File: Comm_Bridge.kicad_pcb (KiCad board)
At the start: 2 copper layers, 66 x 55.9 mm, 98 parts, among them P1 USB_B, P2 CONN_01X03, P3 Solenoid, P4 XT60, P5 CONN_01X03, P6 CONN_01X03, U1 FT4232H, U10 ADM3251E, U11 ADM3251E, U2 93LC56BT-I/OT, U3 74HC595_CUST, U4 LM1117-XX, U5 ADC101S021, U6 NLSX4373, U7 NLSX4373, U8 ACPL-247-500E, U9 ACPL-247-500E, Y1 12MHz

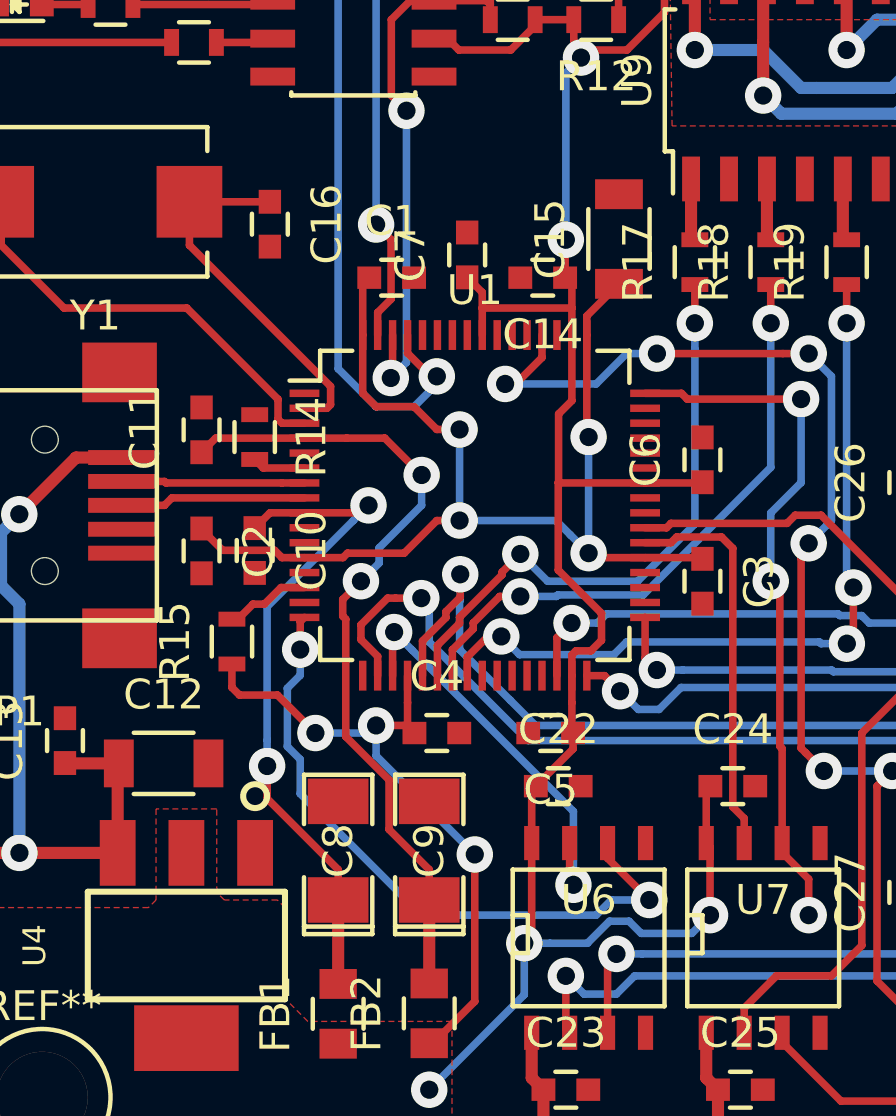
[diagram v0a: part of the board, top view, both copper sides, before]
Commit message: Change the PCB footprints of C4.7uF and 3.3uF from 1206 to 0803 (smaller)
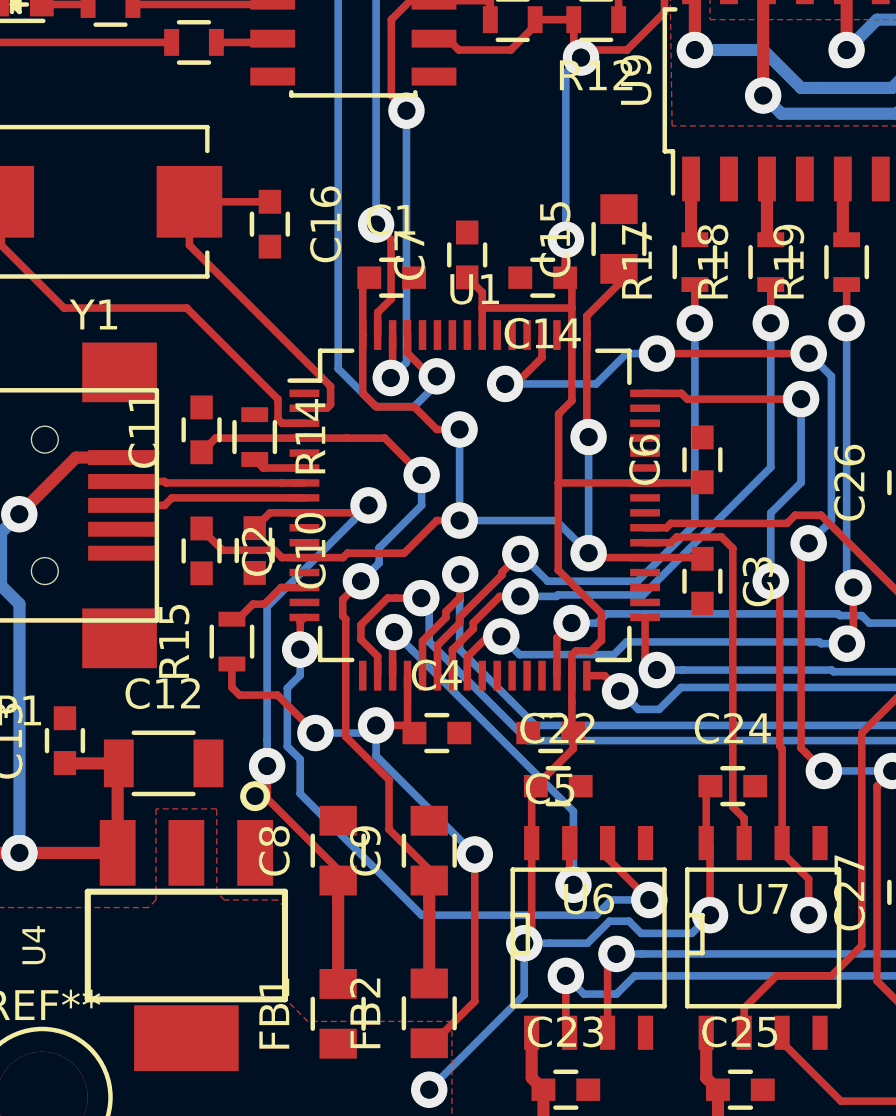
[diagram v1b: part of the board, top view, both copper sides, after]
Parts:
- C15: footprint Capacitors_SMD:C_1206 -> Capacitors_SMD:C_0805
- C8, C9: footprint SMD_Packages:SMD-1206_Pol -> Capacitors_SMD:C_0805
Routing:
- net +1V8: track 38.5 -> 39.0 mm

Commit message: Change the version of KiCad to 4.0.6 and un-connected ID_Pin of the USB connector.
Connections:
- P1 pad 4: GND -> Net-(P1-Pad4)
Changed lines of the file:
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@@
-(kicad_pcb (version 4) (host pcbnew 4.0.5)
+(kicad_pcb (version 4) (host pcbnew 4.0.6)
   (general
-    (links 252)
+    (links 251)
     (no_connects 0)
     (area 118.2798 76.124999 185.785401 132.232402)
@@
     (zones 0)
     (modules 98)
-    (nets 113)
+    (nets 114)
   )
   (page A4)
@@
   (net 111 "Net-(U1-Pad59)")
   (net 112 "Net-(U1-Pad60)")
+  (net 113 "Net-(P1-Pad4)")
   (net_class Default "This is the default net class."
     (clearance 0.2032)
@@
     (add_net "Net-(P1-Pad2)")
     (add_net "Net-(P1-Pad3)")
+    (add_net "Net-(P1-Pad4)")
     (add_net "Net-(P5-Pad2)")
     (add_net "Net-(P5-Pad3)")
@@
       (net 42 "Net-(P1-Pad3)"))
     (pad 4 smd rect (at 3.44932 0.8001) (size 2.30124 0.50038) (layers F.Cu F.Paste F.Mask)
-      (net 2 GND))
+      (net 113 "Net-(P1-Pad4)"))
     (pad 5 smd rect (at 3.44932 1.6002) (size 2.30124 0.50038) (layers F.Cu F.Paste F.Mask)
       (net 2 GND))

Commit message: Merge branch 'Peripheral_Bridge'
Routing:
- net GND: track 8.38 -> 69.5 mm
- net Net-(R13-Pad1): track 30.1 -> 31.9 mm
- net VBUS: track 181.5 -> 180.0 mm
- net Net-(R11-Pad1): track 23.4 -> 24.5 mm
- net Net-(C10-Pad1): track 22.5 -> 21.6 mm
- net Net-(C11-Pad1): track 27.4 -> 26.6 mm

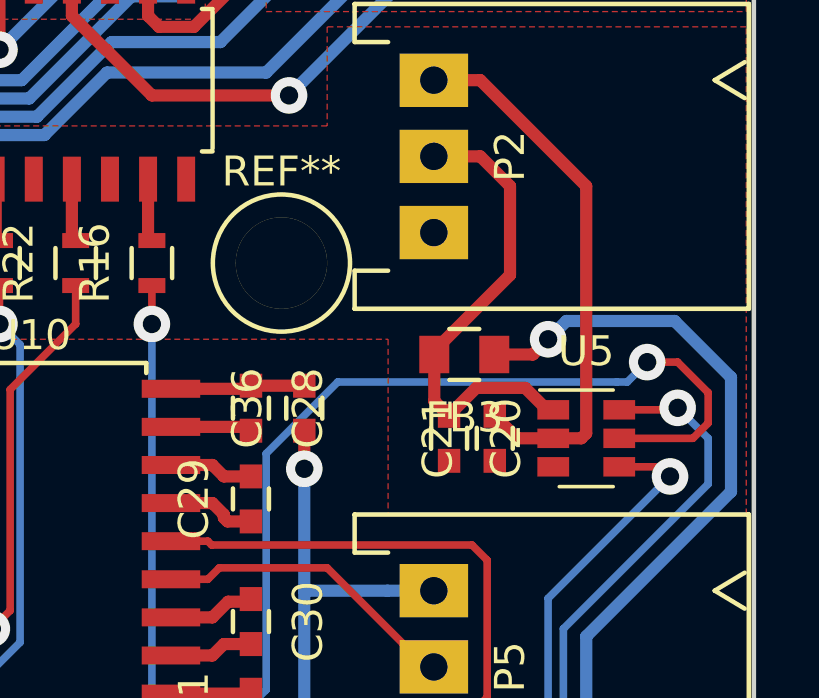
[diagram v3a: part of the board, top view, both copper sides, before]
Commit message: ADC bug fixed
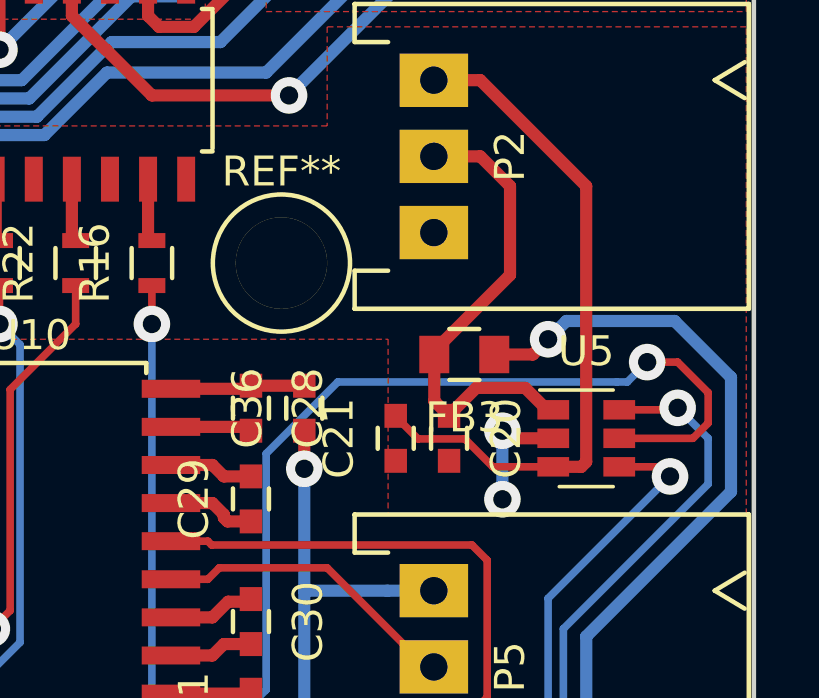
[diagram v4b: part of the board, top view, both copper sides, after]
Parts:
- moved C21 3.30 mm to (173.5, 104.6)
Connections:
- U5 pad 2: Net-(C21-Pad2) -> GND
- U5 pad 3: GND -> Net-(C21-Pad2)
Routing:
- net Net-(C21-Pad2): track 18.2 -> 22.9 mm
- net GND: track 69.5 -> 73.6 mm, vias 2 -> 4
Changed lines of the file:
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@@
     (thickness 1.6)
     (drawings 5)
-    (tracks 888)
+    (tracks 896)
     (zones 0)
     (modules 98)
@@
   )
   (setup
-    (last_trace_width 0.254)
+    (last_trace_width 0.4064)
     (user_trace_width 0.4064)
     (user_trace_width 1.27)
@@
   )
   (module Capacitors_SMD:C_0603 (layer F.Cu)
-    (at 176.784 104.648 90)
+    (at 173.482 104.648 90)
     (descr "Capacitor SMD 0603, reflow soldering, AVX (see smccp.pdf)")
     (tags "capacitor 0603")
@@
       (net 7 "Net-(C20-Pad1)"))
     (pad 2 smd rect (at -1.1 0) (size 1.06 0.65) (layers F.Cu F.Paste F.Mask)
-      (net 8 "Net-(C21-Pad2)"))
-    (pad 3 smd rect (at -1.1 0.95) (size 1.06 0.65) (layers F.Cu F.Paste F.Mask)
       (net 2 GND))
+    (pad 3 smd rect (at -1.1 0.95) (size 1.06 0.65) (layers F.Cu F.Paste F.Mask)
+      (net 8 "Net-(C21-Pad2)"))
     (pad 4 smd rect (at 1.1 0.95) (size 1.06 0.65) (layers F.Cu F.Paste F.Mask)
       (net 77 "Net-(U5-Pad4)"))
@@
   (segment (start 133.246 108.684) (end 133.000201 108.438201) (width 0.254) (layer F.Cu) (net 1))
   (segment (start 131.261201 108.438201) (end 130.556 107.733) (width 0.254) (layer F.Cu) (net 1))
+  (segment (start 177.038 104.394) (end 177.038 106.68) (width 0.4064) (layer B.Cu) (net 2))
+  (via (at 177.038 106.68) (size 1.2192) (drill 0.6096) (layers F.Cu B.Cu) (net 2))
+  (segment (start 178.732 104.648) (end 177.292 104.648) (width 0.4064) (layer F.Cu) (net 2))
+  (segment (start 177.292 104.648) (end 177.038 104.394) (width 0.4064) (layer F.Cu) (net 2))
+  (via (at 177.038 104.394) (size 1.2192) (drill 0.6096) (layers F.Cu B.Cu) (net 2))
   (segment (start 149.710138 123.444) (end 150.4315 123.444) (width 0.254) (layer F.Cu) (net 2))
   (segment (start 151.257 124.2695) (end 151.257 124.587) (width 0.254) (layer F.Cu) (net 2))
@@
   (segment (start 174.768 101.854) (end 174.768 103.406) (width 0.4064) (layer F.Cu) (net 7))
   (segment (start 174.768 103.406) (end 175.26 103.898) (width 0.4064) (layer F.Cu) (net 7))
-  (segment (start 179.832 96.2406) (end 179.832 104.4844) (width 0.4064) (layer F.Cu) (net 8))
-  (segment (start 179.832 104.4844) (end 179.6684 104.648) (width 0.4064) (layer F.Cu) (net 8))
-  (segment (start 179.6684 104.648) (end 178.732 104.648) (width 0.4064) (layer F.Cu) (net 8))
+  (segment (start 175.787799 104.667799) (end 176.718 105.598) (width 0.254) (layer F.Cu) (net 8))
+  (segment (start 176.718 105.598) (end 178.732 105.598) (width 0.254) (layer F.Cu) (net 8))
+  (segment (start 173.482 103.898) (end 173.482 103.923) (width 0.254) (layer F.Cu) (net 8))
+  (segment (start 173.482 103.923) (end 174.226799 104.667799) (width 0.254) (layer F.Cu) (net 8))
+  (segment (start 174.226799 104.667799) (end 175.787799 104.667799) (width 0.254) (layer F.Cu) (net 8))
+  (segment (start 179.832 96.2406) (end 179.832 105.4344) (width 0.4064) (layer F.Cu) (net 8))
+  (segment (start 179.832 105.4344) (end 179.6684 105.598) (width 0.4064) (layer F.Cu) (net 8))
+  (segment (start 179.6684 105.598) (end 178.732 105.598) (width 0.4064) (layer F.Cu) (net 8))
   (segment (start 174.752 92.71) (end 176.3014 92.71) (width 0.4064) (layer F.Cu) (net 8))
   (segment (start 176.3014 92.71) (end 179.832 96.2406) (width 0.4064) (layer F.Cu) (net 8))
-  (segment (start 176.784 103.898) (end 177.534 104.648) (width 0.4064) (layer F.Cu) (net 8))
-  (segment (start 177.534 104.648) (end 178.732 104.648) (width 0.4064) (layer F.Cu) (net 8))
   (segment (start 168.656 102.894) (end 170.434 102.894) (width 0.4064) (layer F.Cu) (net 9))
   (segment (start 165.99 102.997) (end 168.553 102.997) (width 0.4064) (layer F.Cu) (net 9))

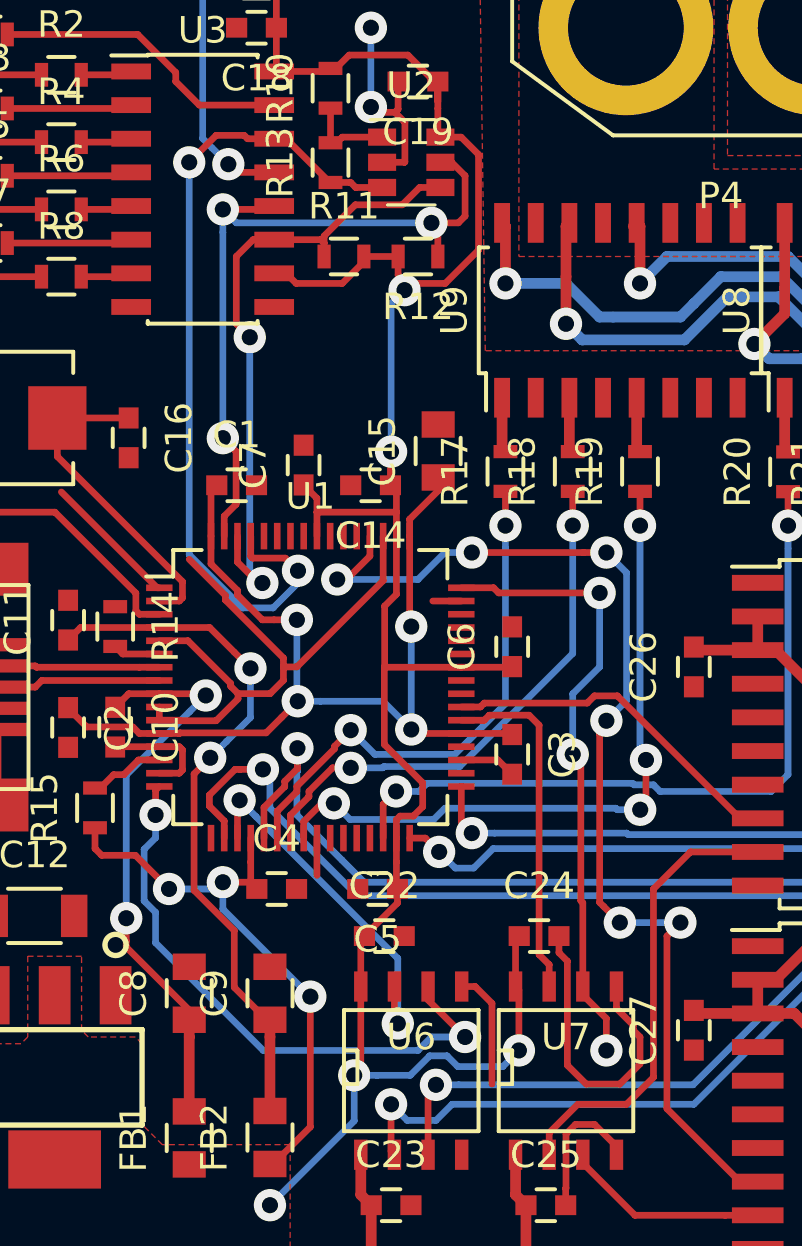
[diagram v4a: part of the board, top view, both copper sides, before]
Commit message: Bug fixed at 74HC595
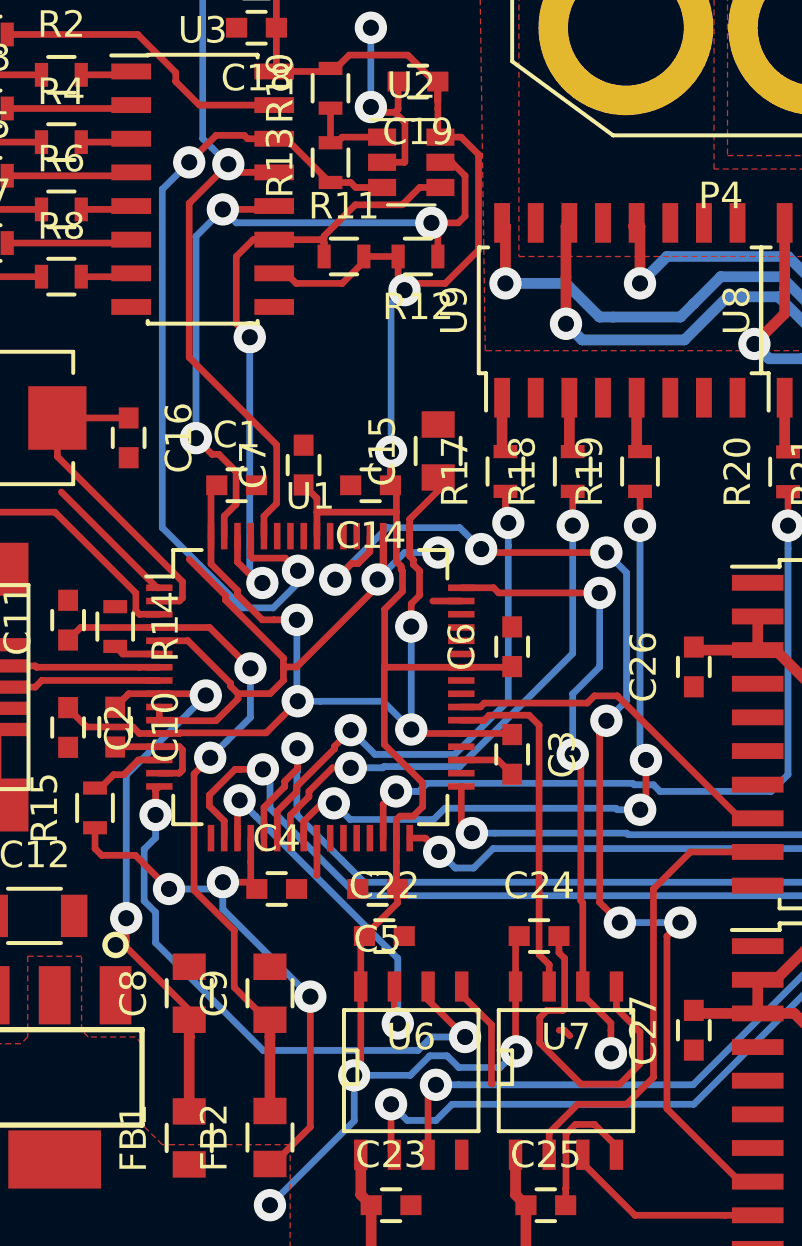
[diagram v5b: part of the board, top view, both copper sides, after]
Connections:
- U1 pad 60: Net-(U1-Pad60) -> Net-(R9-Pad1)
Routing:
- net Net-(R9-Pad1): track 10.5 -> 26.7 mm
- net GND: track 73.6 -> 79.0 mm, vias 4 -> 6
- net Net-(R12-Pad1): track 28.2 -> 29.6 mm
- net Net-(U1-Pad52): track 42.0 -> 42.9 mm
- net Net-(R13-Pad1): track 31.9 -> 32.7 mm

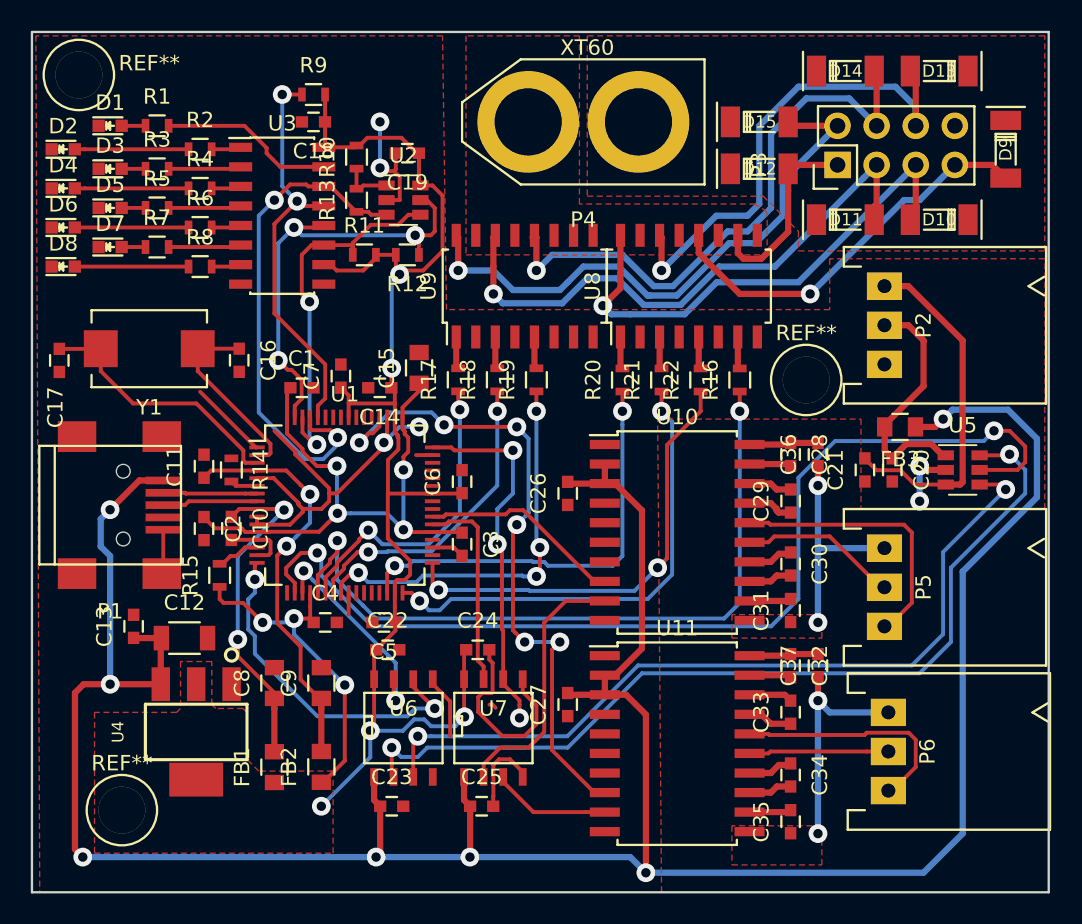
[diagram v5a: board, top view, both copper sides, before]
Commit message: Bug fixed at NLSX4373 (Level Shifter)
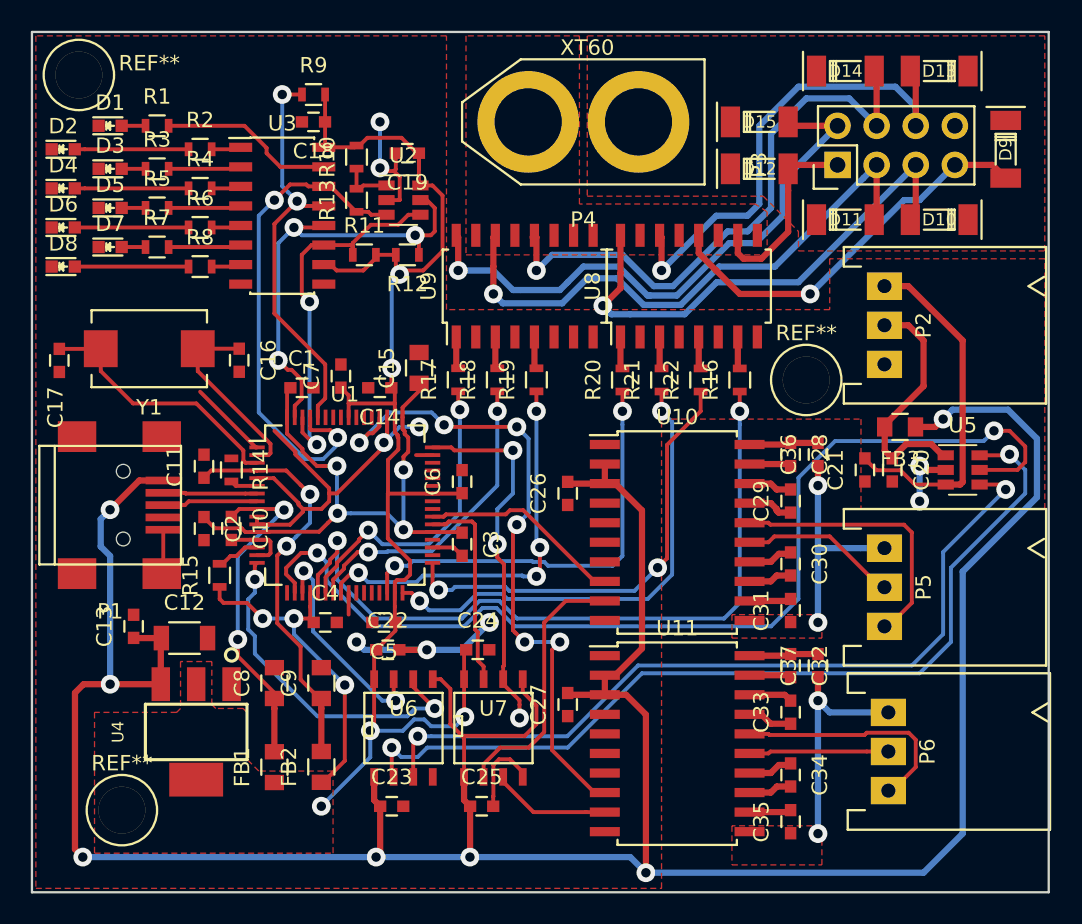
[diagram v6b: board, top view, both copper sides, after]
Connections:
- U6 pad 5: GND -> VBUS
- U7 pad 5: GND -> VBUS
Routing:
- net VBUS: track 180.0 -> 196.3 mm
- net GND: track 79.0 -> 73.3 mm, vias 6 -> 9
- net Net-(U1-Pad18): track 67.4 -> 68.4 mm
- net Net-(R16-Pad1): track 47.8 -> 48.8 mm
- net Net-(U1-Pad19): track 13.8 -> 14.3 mm

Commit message: Change REF resistor from 10k to 12k 1%
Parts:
- R14: value 10k -> 12k 1%
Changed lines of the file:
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@@
     (links 252)
     (no_connects 0)
-    (area 116.88 73.7 185.785401 132.232402)
+    (area 119.304999 76.124999 185.495001 132.155001)
     (thickness 1.6)
     (drawings 5)
@@
       (effects (font (size 1 1) (thickness 0.15)))
     )
-    (fp_text value 10k (at 0 1.9 270) (layer F.Fab)
-      (effects (font (size 1 1) (thickness 0.15)))
-    )
+    (fp_text value "12k 1%" (at 0 1.9 270) (layer F.Fab)
+      (effects (font (size 1 1) (thickness 0.15)))
+    )
